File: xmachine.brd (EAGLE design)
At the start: 125 x 100 mm, 2 parts, among them IC1 ECP5-LFE5U-XXF-8BG381C, J1 PDS-030

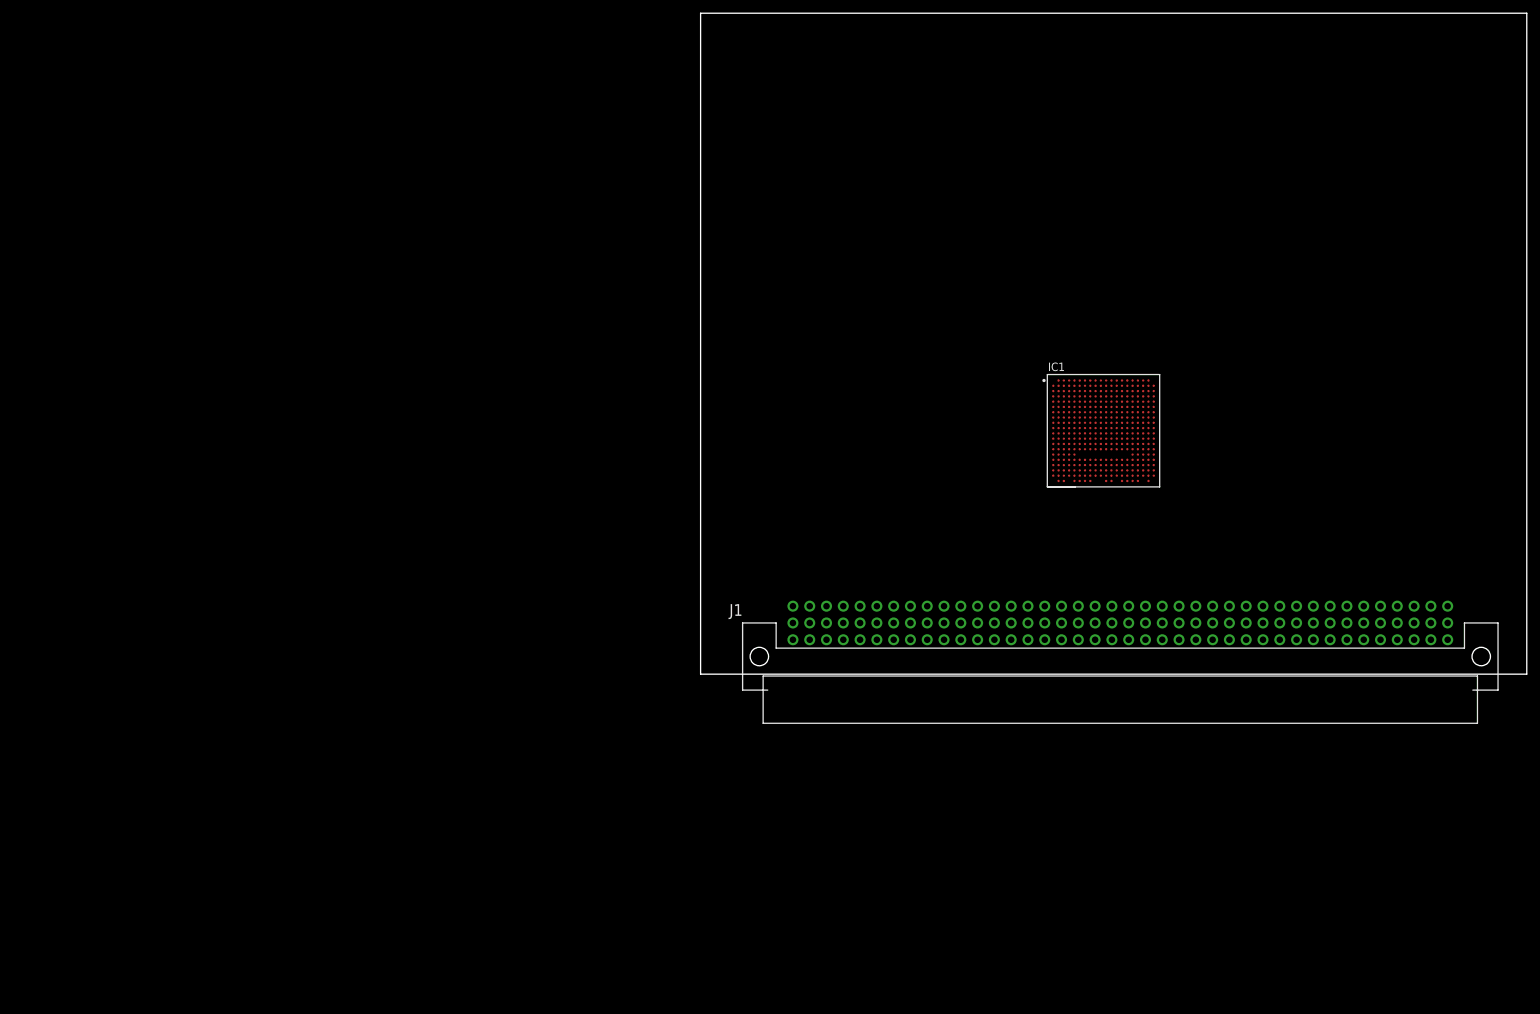
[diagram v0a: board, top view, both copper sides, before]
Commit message: added level shifters and flash memory
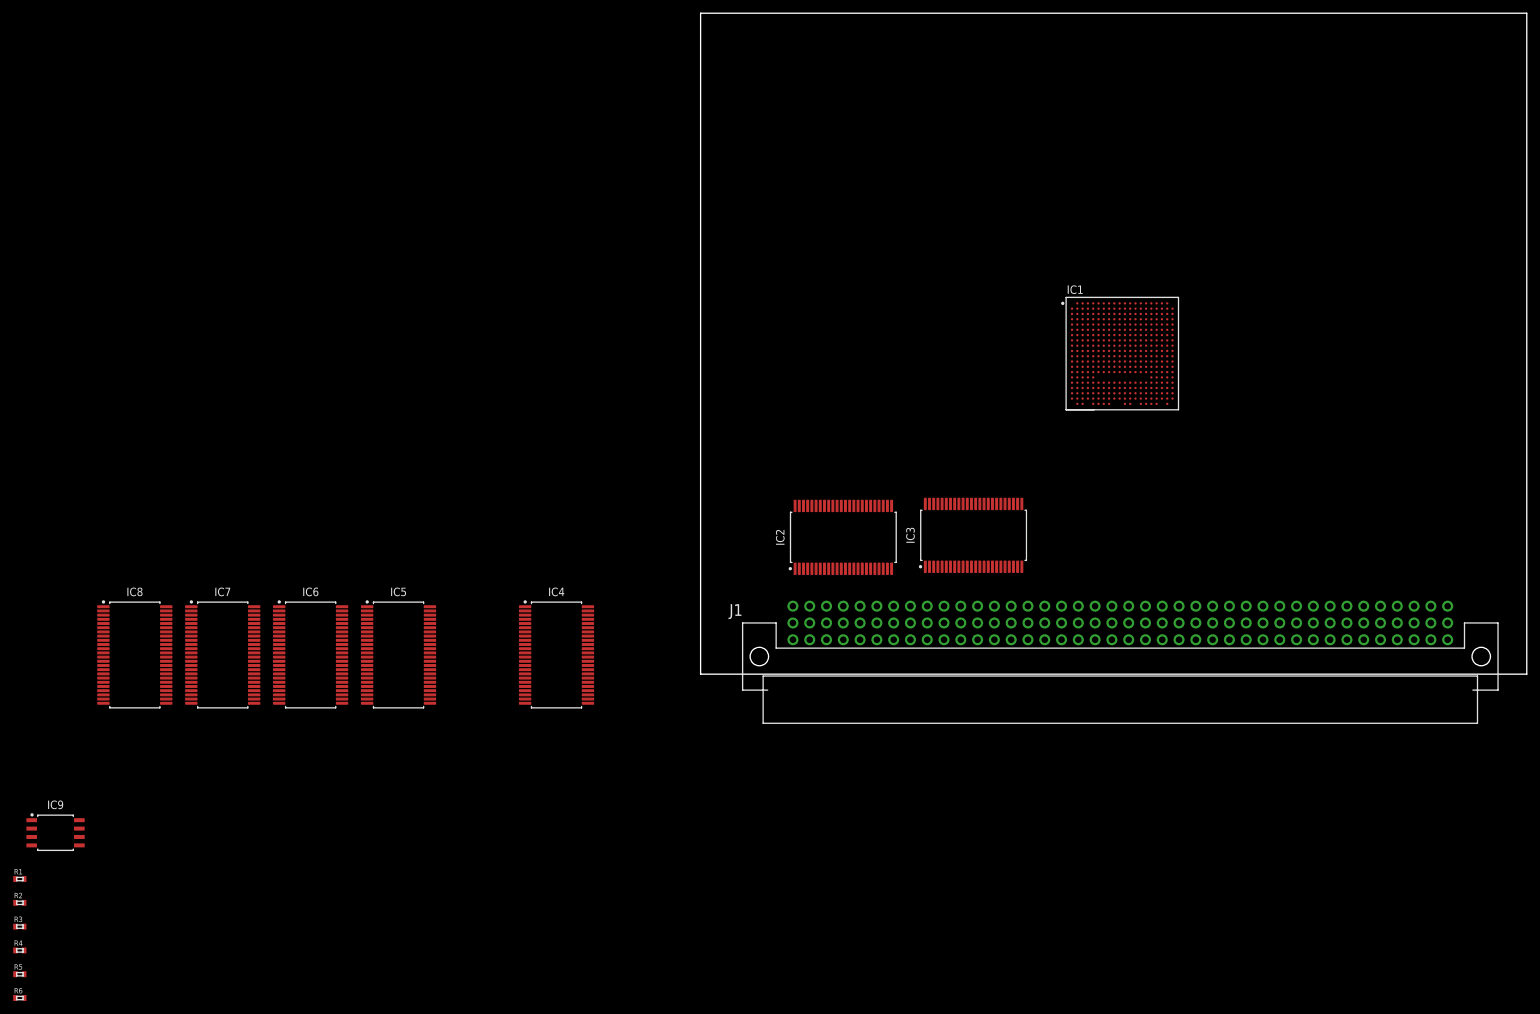
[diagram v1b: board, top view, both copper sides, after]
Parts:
- added IC2, IC3, IC4, IC5, IC6, IC7, IC8: SN74LVC16T245, sk9k-Texas Instruments:SOP63P1035X279-48N
- added IC9: IS25WP128-JBLE, sk9k-Memory:SOIC127P790X216-8N
- added R1, R2, R3, R4: 10k, sk9k-RCL:R0402
- added R5: 1k, sk9k-RCL:R0402
- added R6: 4.7k, sk9k-RCL:R0402
- moved IC1 12.0 mm to (63.8, 48.5)
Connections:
- new net /BG: IC6.2, J1.B10
- new net /BGACK: IC7.3, J1.A10
- new net /BR: IC7.2, J1.C10
- new net /BUSLOCK: IC7.11, J1.A3
- new net /CBACK: IC7.6, J1.B7
- new net /CBREQ: IC6.3, J1.C7
- new net /CIOUT: IC6.5, J1.A6
- new net /IRQ1: J1.C4
- new net /IRQ2: J1.B4
- new net /IRQ3: J1.A4
- new net /NUBUS: IC6.8, J1.C2
- new net /RMC: IC6.6, J1.C6
- new net /STERM: IC7.5, J1.A7
- new net /TM0A: IC7.8, J1.C3
- new net /TM1A: IC7.9, J1.B3
- new net 3V3: IC2.31, IC2.42, IC3.31, IC3.42, IC4.31, IC4.42, IC5.31, IC5.42, IC6.31, IC6.42, IC7.1, IC7.24, IC7.31, IC7.42, IC9.8, R1.2, R2.2, R3.2, R4.2, R5.2, R6.2
- new net 5V: IC2.18, IC2.7, IC3.18, IC3.7, IC4.18, IC4.7, IC5.18, IC5.7, IC6.18, IC6.7, IC7.18, IC7.7, J1.A37, J1.B13, J1.B19, J1.B25, J1.B31, J1.B37, J1.C37
- new net A0: IC2.2, J1.C36
- new net A1: IC2.3, J1.B36
- new net A10: IC2.16, J1.A33
- new net A11: IC2.17, J1.C32
- new net A12: IC2.19, J1.B32
- new net A13: IC2.20, J1.A32
- new net A14: IC2.22, J1.C31
- new net A15: IC2.23, J1.A31
- new net A16: IC3.2, J1.C30
- new net A17: IC3.3, J1.B30
- new net A18: IC3.5, J1.A30
- new net A19: IC3.6, J1.C29
- new net A2: IC2.5, J1.A36
- new net A20: IC3.8, J1.B29
- new net A21: IC3.9, J1.A29
- new net A22: IC3.11, J1.C28
- new net A23: IC3.12, J1.A28
- new net A24: IC3.13, J1.C27
- new net A25: IC3.14, J1.B27
- new net A26: IC3.16, J1.A27
- new net A27: IC3.17, J1.C26
- new net A28: IC3.19, J1.B26
- new net A29: IC3.20, J1.A26
- new net A3: IC2.6, J1.C35
- new net A30: IC3.22, J1.C25
- new net A31: IC3.23, J1.A25
- new net A4: IC2.8, J1.B35
- new net A5: IC2.9, J1.A35
- new net A6: IC2.11, J1.C34
- new net A7: IC2.12, J1.A34
- new net A8: IC2.13, J1.C33
- new net A9: IC2.14, J1.B33
- new net ADDR_DIR: IC2.1, IC2.24, IC3.1, IC3.24
- new net C16M: IC6.13, J1.C38
- new net CPUCLK: IC6.11, J1.A38
- new net DATA_DIR: IC4.1, IC4.24, IC5.1, IC5.24
- new net ECLK: IC6.12, J1.B38
- new net FLASH_CLK: IC9.6, R5.1
- new net FLASH_CS: IC9.1, R6.1
- new net FLASH_HOLD: IC9.7, R2.1
- new net FLASH_MISO: IC9.2, R3.1
- new net FLASH_MOSI: IC9.5, R4.1
- new net FLASH_WP: IC9.3, R1.1
- new net GND: IC2.10, IC2.15, IC2.21, IC2.25, IC2.28, IC2.34, IC2.39, IC2.4, IC2.45, IC2.48, IC3.10, IC3.15, IC3.21, IC3.25, IC3.28, IC3.34, IC3.39, IC3.4, IC3.45, IC3.48, IC4.10, IC4.15, IC4.21, IC4.25, IC4.28, IC4.34, IC4.39, IC4.4, IC4.45, IC4.48, IC5.10, IC5.15, IC5.21, IC5.25, IC5.28, IC5.34, IC5.39, IC5.4, IC5.45, IC5.48, IC6.1, IC6.10, IC6.15, IC6.21, IC6.24, IC6.28, IC6.34, IC6.39, IC6.4, IC6.45, IC6.48, IC7.10, IC7.15, IC7.21, IC7.25, IC7.28, IC7.34, IC7.39, IC7.4, IC7.45, IC7.48, IC9.4, J1.A39, J1.B16, J1.B2, J1.B22, J1.B28, J1.B34, J1.B39, J1.C39
- new net N$100: IC2.43
- new net N$101: J1.A1
- new net N$102: J1.A2
- new net N$103: J1.B1
- new net N$107: J1.C5
- new net N$110: J1.C8
- new net N$111: J1.C9
- new net N$113: IC2.41
- new net N$114: IC2.40
- new net N$115: IC2.38
- new net N$116: IC2.37
- new net N$118: IC2.36
- new net N$119: IC2.35
- new net N$120: IC2.33
- new net N$122: IC2.32
- new net N$123: IC2.30
- new net N$124: IC2.29
- new net N$125: IC2.27
- new net N$126: IC2.26
- new net N$150: IC3.47
- new net N$151: IC3.46
- new net N$152: IC3.44
- new net N$153: IC3.43
- new net N$154: IC3.41
- new net N$155: IC3.40
- new net N$156: IC3.38
- new net N$157: IC3.37
- new net N$159: IC3.36
- new net N$160: IC3.35
- new net N$162: IC3.33
- new net N$163: IC3.32
- new net N$164: IC3.30
- new net N$165: IC3.29
- new net N$166: IC3.27
- new net N$167: IC3.26
- new net N$190: IC5.2
- new net N$191: IC5.3
- new net N$192: IC5.5
- new net N$193: IC5.6
- new net N$194: IC5.8
- new net N$195: IC5.9
- new net N$196: IC5.11
- new net N$197: IC5.12
- new net N$199: IC5.13
- new net N$200: IC5.14
- new net N$202: IC5.16
- new net N$203: IC5.17
- new net N$204: IC5.19
- new net N$205: IC5.20
- new net N$206: IC5.22
- new net N$207: IC5.23
- new net N$209: IC5.47
- new net N$210: IC5.46
- new net N$211: IC5.44
- new net N$212: IC5.43
- new net N$213: IC5.41
- new net N$214: IC5.40
- new net N$215: IC5.38
- new net N$216: IC5.37
- new net N$218: IC5.36
- new net N$219: IC5.35
- new net N$220: IC5.33
- new net N$222: IC5.32
- new net N$223: IC5.30
- new net N$224: IC5.29
- new net N$225: IC5.27
- new net N$226: IC5.26
- new net N$229: IC4.47
- new net N$230: IC4.46
- new net N$231: IC4.44
- new net N$232: IC4.43
- new net N$233: IC4.41
- new net N$234: IC4.40
- new net N$235: IC4.38
- new net N$236: IC4.37
- new net N$238: IC4.36
- new net N$239: IC4.35
- new net N$240: IC4.33
- new net N$242: IC4.32
- new net N$243: IC4.30
- new net N$244: IC4.29
- new net N$245: IC4.27
- new net N$246: IC4.26
- new net N$250: IC4.2
- new net N$251: IC4.3
- new net N$252: IC4.5
- new net N$253: IC4.6
- new net N$254: IC4.8
- new net N$255: IC4.9
- new net N$256: IC4.11
- new net N$257: IC4.12
- new net N$259: IC4.13
- new net N$260: IC4.14
- new net N$262: IC4.16
- new net N$263: IC4.17
- new net N$264: IC4.19
- new net N$265: IC4.20
- new net N$266: IC4.22
- new net N$267: IC4.23
- new net N$270: IC6.47
- new net N$271: IC6.46
- new net N$272: IC6.44
- new net N$273: IC6.43
- new net N$274: IC6.41
- new net N$275: IC6.40
- new net N$276: IC6.38
- new net N$277: IC6.37
- new net N$279: IC6.36
- new net N$280: IC6.35
- new net N$282: IC6.33
- new net N$283: IC6.32
- new net N$284: IC6.30
- new net N$285: IC6.29
- new net N$286: IC6.27
- new net N$287: IC6.26
- new net N$298: IC6.25
- new net N$307: IC7.12
- new net N$309: IC7.47
- new net N$310: IC7.46
- new net N$311: IC7.44
- new net N$312: IC7.43
- new net N$313: IC7.41
- new net N$314: IC7.40
- new net N$315: IC7.38
- new net N$316: IC7.37
- new net N$318: IC7.36
- new net N$319: IC7.35
- new net N$320: IC7.33
- new net N$322: IC7.32
- new net N$323: IC7.30
- new net N$324: IC7.29
- new net N$325: IC7.27
- new net N$326: IC7.26
- new net N$339: IC7.13
- new net N$340: IC7.14
- new net N$342: IC7.16
- new net N$343: IC7.17
- new net N$344: IC7.19
- new net N$345: IC7.20
- new net N$346: IC7.22
- new net N$347: IC7.23
- new net N$348: IC8.1
- new net N$349: IC8.47
- new net N$35: J1.A5
- new net N$350: IC8.46
- new net N$351: IC8.44
- new net N$352: IC8.43
- new net N$353: IC8.41
- new net N$354: IC8.40
- new net N$355: IC8.38
- new net N$356: IC8.37
- new net N$357: IC8.24
- new net N$358: IC8.36
- new net N$359: IC8.35
- new net N$360: IC8.33
- new net N$362: IC8.32
- new net N$363: IC8.30
- new net N$364: IC8.29
- new net N$365: IC8.27
- new net N$366: IC8.26
- new net N$367: IC8.10, IC8.15, IC8.21, IC8.28, IC8.34, IC8.39, IC8.4, IC8.45
- new net N$368: IC8.18, IC8.7
- new net N$369: IC8.48
- new net N$370: IC8.2
- new net N$371: IC8.3
- new net N$372: IC8.5
- new net N$373: IC8.6
- new net N$374: IC8.8
- new net N$375: IC8.9
- new net N$376: IC8.11
- new net N$377: IC8.12
- new net N$378: IC8.25
- new net N$379: IC8.13
- new net N$38: J1.A8
- new net N$380: IC8.14
- new net N$382: IC8.16
- new net N$383: IC8.17
- new net N$384: IC8.19
- new net N$385: IC8.20
- new net N$386: IC8.22
- new net N$387: IC8.23
- new net N$4: IC6.17
- new net N$40: J1.A13
- new net N$41: J1.C13
- new net N$42: J1.A14
- new net N$43: J1.B14
- new net N$44: J1.C14
- new net N$45: J1.A15
- new net N$46: J1.B15
- new net N$47: J1.C15
- new net N$48: J1.A16
- new net N$49: J1.C16
- new net N$5: IC6.19
- new net N$50: J1.A17
- new net N$51: J1.B17
- new net N$52: J1.C17
- new net N$53: J1.A18
- new net N$54: J1.B18
- new net N$55: J1.C18
- new net N$56: J1.A19
- new net N$57: J1.C19
- new net N$58: J1.A20
- new net N$59: J1.B20
- new net N$6: IC6.20
- new net N$60: J1.C20
- new net N$61: J1.A21
- new net N$62: J1.B21
- new net N$63: J1.C21
- new net N$64: J1.A22
- new net N$65: J1.C22
- new net N$66: J1.A23
- new net N$67: J1.B23
- new net N$68: J1.C23
- new net N$69: J1.A24
- new net N$7: IC6.22
- new net N$70: J1.B24
- new net N$71: J1.C24
- new net N$73: J1.A11
- new net N$74: J1.A12
- new net N$78: J1.B5
- new net N$79: J1.B6
- new net N$8: IC6.23
- new net N$81: J1.B8
- new net N$84: J1.B11
- new net N$85: J1.B12
- new net N$89: IC2.47
- new net N$90: IC2.46
- new net N$91: J1.C11
- new net N$92: J1.C12
- new net N$94: IC2.44
- new net N$96: J1.B40
- new net N$97: J1.C40
- new net N$98: J1.A40
- new net POWEROFF: IC6.9
- new net PWROFF: J1.C1
- new net SIZ0: J1.B9
- new net SIZ1: J1.A9
